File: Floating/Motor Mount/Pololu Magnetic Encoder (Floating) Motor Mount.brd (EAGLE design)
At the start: 26.7 x 33.7 mm, 0 parts

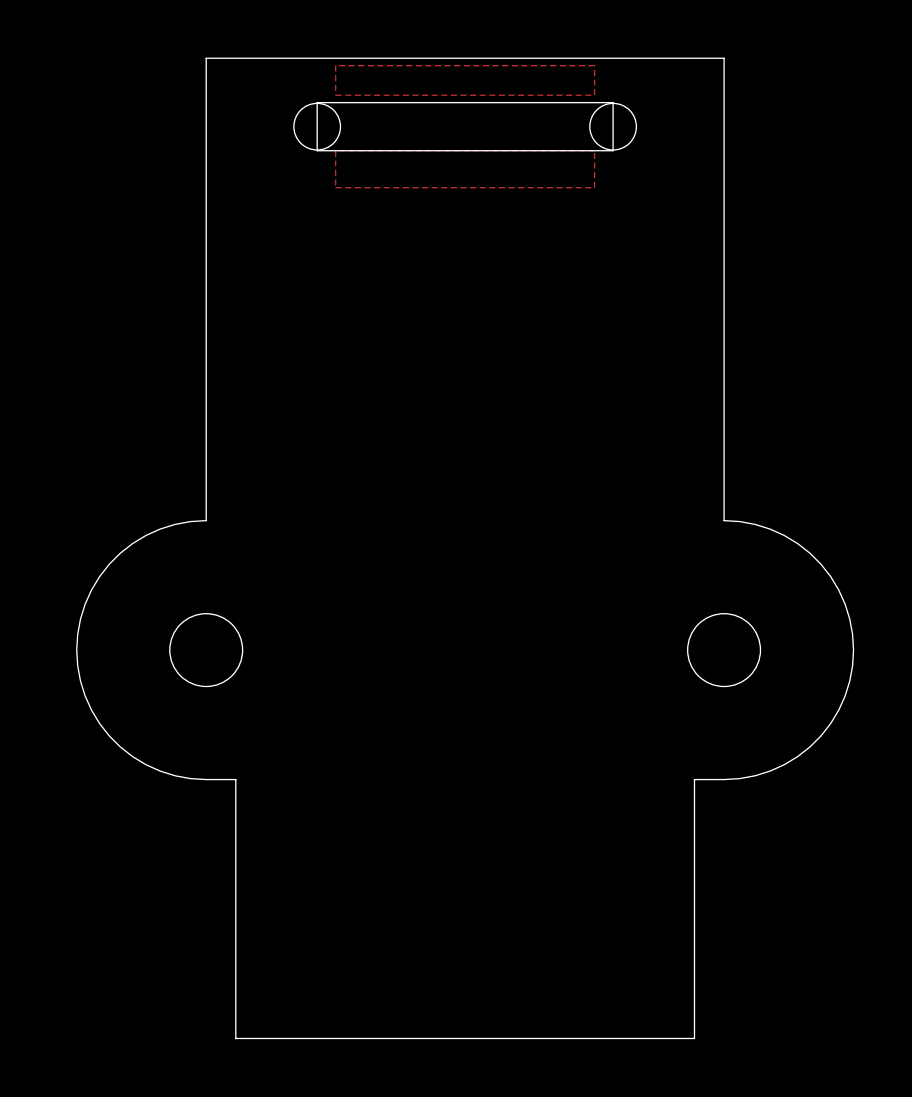
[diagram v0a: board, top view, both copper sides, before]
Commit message: Messing with encoders. Created base plate for Black Mount Created two PCBs for base-less/floating encoder
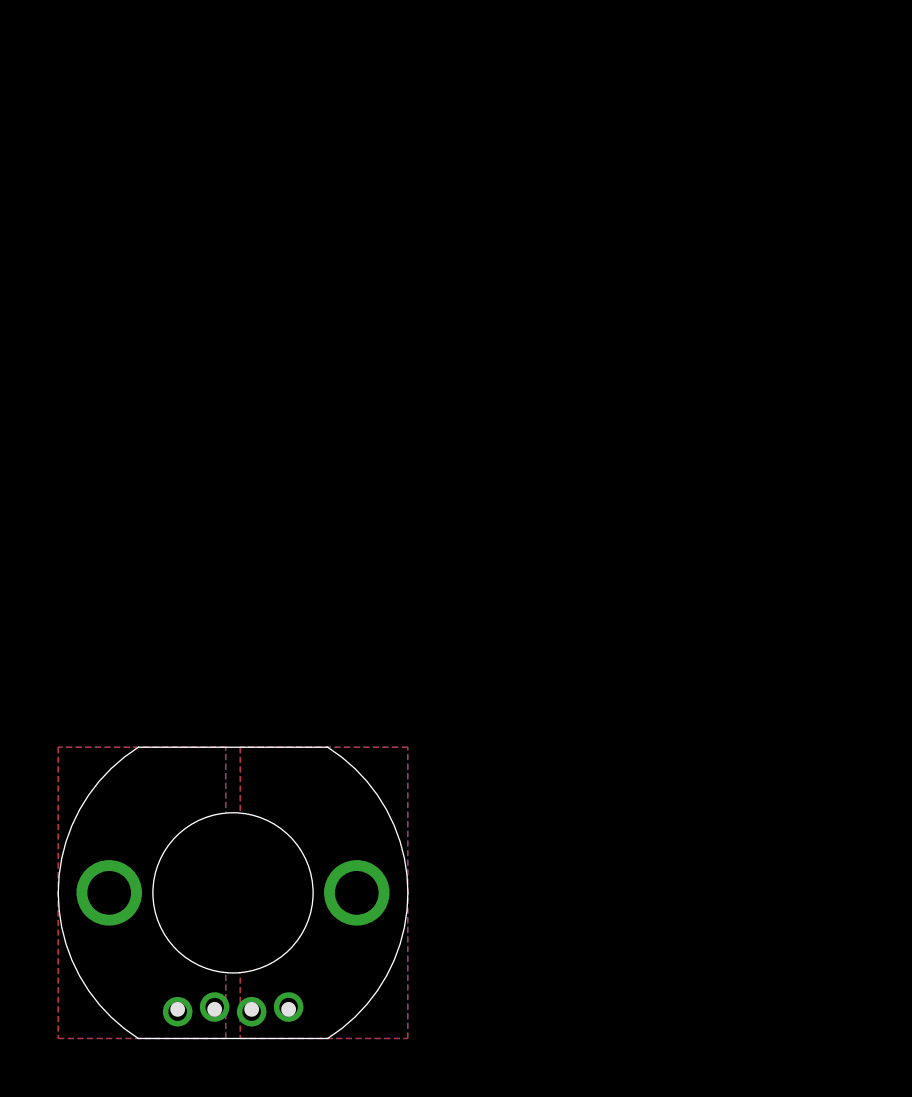
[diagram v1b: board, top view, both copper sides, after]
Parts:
- added U$1: 1X4.LOCK, headers(.05in):1X4.LOCK
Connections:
- new net M+: U$1.1, U$1.2
- new net M-: U$1.3, U$1.4
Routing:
- added copper zone on layer 1, net M+
- added copper zone on layer 16, net M+
- added copper zone on layer 1, net M-
- added copper zone on layer 16, net M-
- removed copper zone on layer 1, net GND
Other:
- board size 26.7 x 33.7 mm -> 12 x 10 mm
- board text added: "+"
- board text added: "-"
- board text removed: "3.3v"
- board text removed: "A"
- board text removed: "B"
- board text removed: "Cruz Monrreal II"
- board text removed: "GND"
- board text removed: "innovativemaker.com"

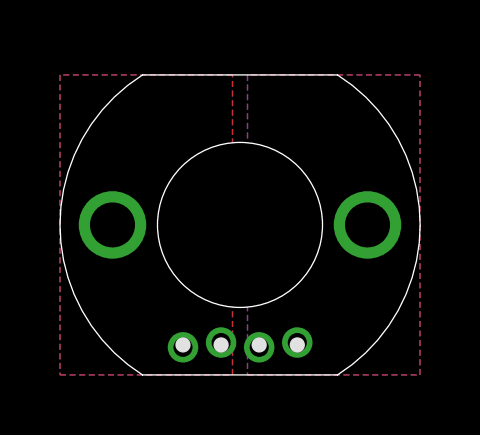
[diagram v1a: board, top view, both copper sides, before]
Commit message: Added decoupling capacitor to motor connetions Made 'oval' vias for motors
All in all, should now fit motors
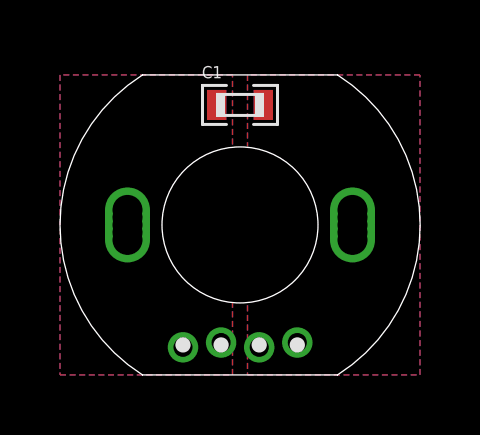
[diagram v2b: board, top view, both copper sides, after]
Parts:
- added C1: .1uF, standardparts:0603
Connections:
- net M+: now also C1.1
- net M-: now also C1.2
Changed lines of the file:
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@@
 <wire x1="9.25" y1="10" x2="2.75" y2="10" width="0" layer="20"/>
 <wire x1="2.75" y1="10" x2="2.75" y2="0" width="0" layer="20" curve="115.243198"/>
-<hole x="6" y="5" drill="5.5"/>
-<text x="1.25" y="4" size="1.778" layer="51" ratio="12" rot="R180" align="bottom-right">+</text>
-<text x="11" y="4" size="1.778" layer="51" ratio="12" rot="R180">-</text>
-<text x="2.5" y="4" size="1.778" layer="52" ratio="12" rot="MR180" align="bottom-right">+</text>
-<text x="9" y="4" size="1.778" layer="52" ratio="12" rot="MR180">-</text>
+<hole x="6" y="5" drill="5.2"/>
+<text x="1.75" y="3.75" size="1.778" layer="51" ratio="12" rot="R180" align="bottom-right">+</text>
+<text x="10.5" y="3.75" size="1.778" layer="51" ratio="12" rot="R180">-</text>
+<text x="3" y="3.75" size="1.778" layer="52" ratio="12" rot="MR180" align="bottom-right">+</text>
+<text x="8.5" y="3.75" size="1.778" layer="52" ratio="12" rot="MR180">-</text>
 <circle x="6" y="5" radius="1.25" width="0.254" layer="51"/>
 </plain>
@@
 <elements>
 <element name="U$1" library="headers(.05in)" package="1X4.LOCK" value="1X4.LOCK" x="4.1" y="1"/>
+<element name="C1" library="standardparts" package="0603" value=".1uF" x="6" y="9"/>
 </elements>
 <signals>
 <signal name="M+">
-<via x="1.75" y="5" extent="1-16" drill="1.5" diameter="2.1844"/>
+<via x="2.25" y="5" extent="1-16" drill="1"/>
 <contactref element="U$1" pad="1"/>
 <contactref element="U$1" pad="2"/>
@@
 <vertex x="0" y="10"/>
 </polygon>
+<contactref element="C1" pad="1"/>
+<via x="2.25" y="5.25" extent="1-16" drill="1"/>
+<via x="2.25" y="5.5" extent="1-16" drill="1"/>
+<via x="2.25" y="4.75" extent="1-16" drill="1"/>
+<via x="2.25" y="4.5" extent="1-16" drill="1"/>
 </signal>
 <signal name="M-">
-<via x="10.25" y="5" extent="1-16" drill="1.5"/>
+<via x="9.75" y="5" extent="1-16" drill="1"/>
 <contactref element="U$1" pad="3"/>
 <contactref element="U$1" pad="4"/>
@@
 <vertex x="6.25" y="10"/>
 </polygon>
+<contactref element="C1" pad="2"/>
+<via x="9.75" y="4.75" extent="1-16" drill="1"/>
+<via x="9.75" y="4.5" extent="1-16" drill="1"/>
+<via x="9.75" y="5.25" extent="1-16" drill="1"/>
+<via x="9.75" y="5.5" extent="1-16" drill="1"/>
 </signal>
 </signals>
